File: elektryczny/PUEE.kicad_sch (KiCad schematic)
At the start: 60 parts, among them J1 CAN, J2 LED2, J3 OLED, J4 Button1, J5 LED1, J6 Button1, J7 Conn_01x05, SW1 Button2, SW2 Button1, U1 STM32F042F4Px, U10 WS2815, U11 WS2815, U13 SN65HVD230QDRG4Q1, U2 ESP-12E, U3 TPS54302DDCR, U4 WS2815, U5 WS2815, U6 WS2815, U7 WS2815, U8 WS2815, U9 WS2815, Y2 ABL-8MHZ-B2

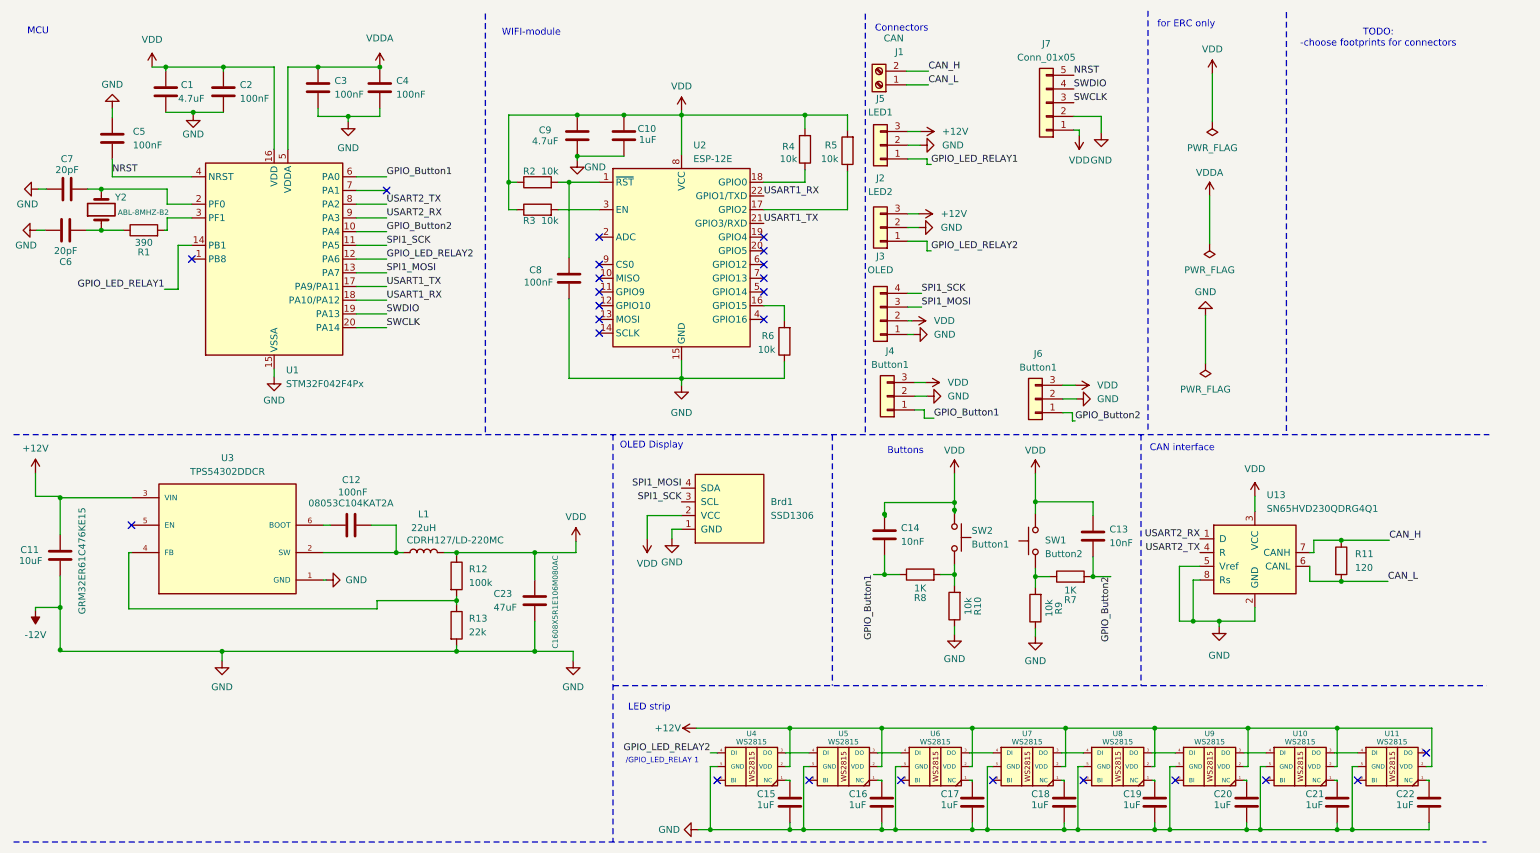
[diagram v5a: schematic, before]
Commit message: poprawa schematu, wymiary sciezek wylotek, pcb film 3.
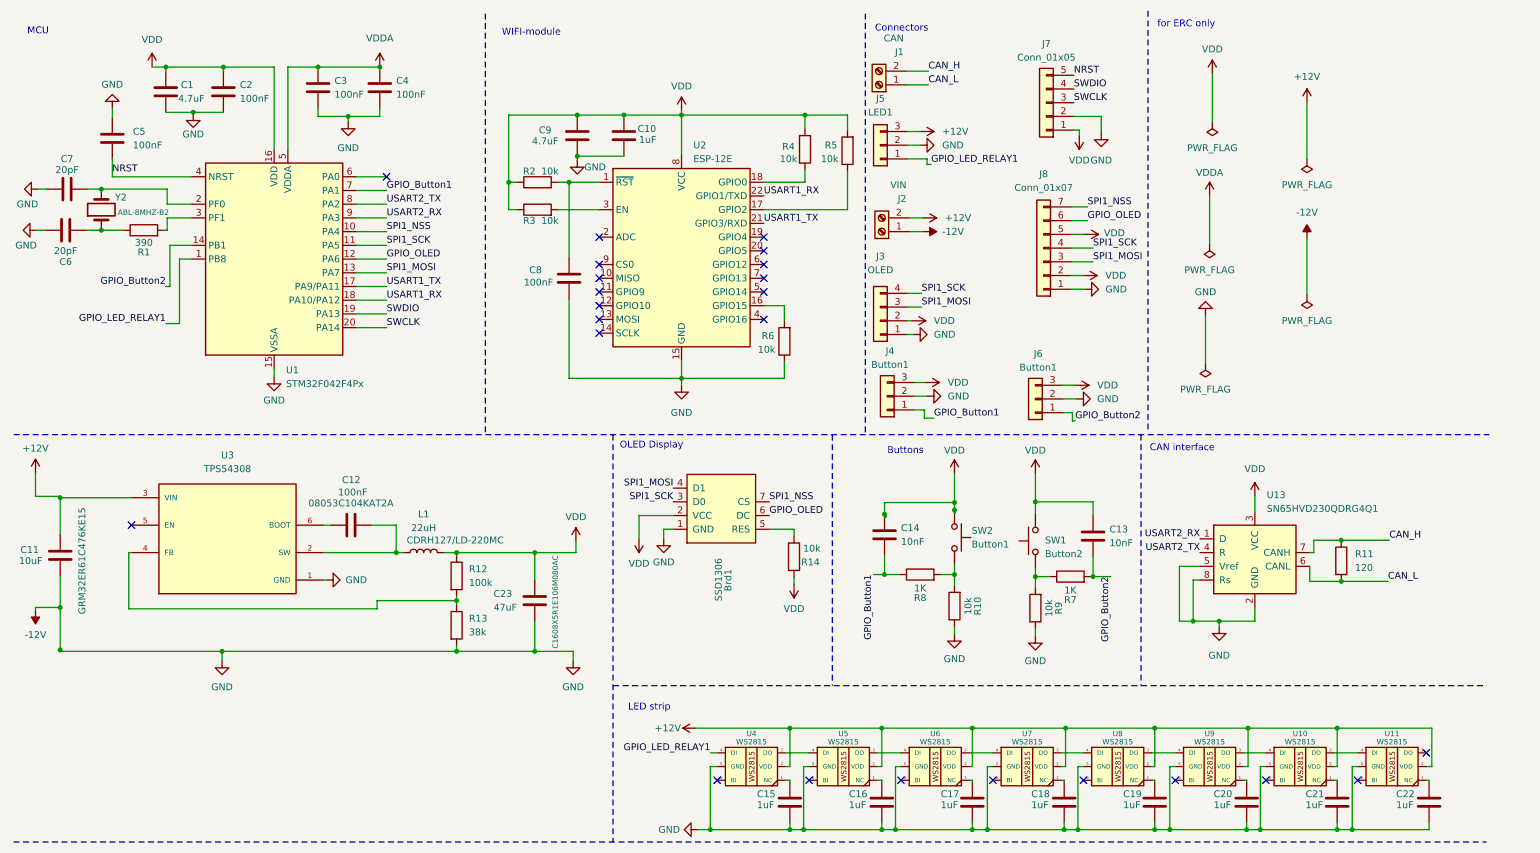
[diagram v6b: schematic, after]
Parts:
- removed J2: LED2, Connector_PinHeader_2.54mm:PinHeader_1x03_P2.54mm_Vertical, symbol Connector_Generic:Conn_01x03
- added J2: VIN, Connector_Phoenix_MC:PhoenixContact_MCV_1,5_2-G-3.5_1x02_P3.50mm_Vertical, symbol Connector:Screw_Terminal_01x02
- added J8: Conn_01x07, Connector_PinHeader_2.54mm:PinHeader_1x07_P2.54mm_Vertical, symbol Connector_Generic:Conn_01x07
- added R14: 10k, Resistor_SMD:R_0805_2012Metric, symbol Device:R
- R13: value 22k -> 38k
- SW1, SW2: footprint (none) -> Button_Switch_SMD:SW_SPST_PTS647_Sx38; Catalogue_number (none) -> PTS647 Series
- U10, U11, U4, U5, U6, U7, U8, U9: footprint WS2815:LED-TRICOLOR-5050 -> LED_SMD:LED_WS2812_PLCC6_5.0x5.0mm_P1.6mm
- U3: value TPS54302DDCR -> TPS54308; footprint TPS54302DDCR:SOT95P280X110-6N -> Package_SO:Texas_HSOP-8-1EP_3.9x4.9mm_P1.27mm
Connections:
- net +12V: now also J2.2 (Pin_2)
- net -12V: now also J2.1 (Pin_1), J8.1 (Pin_1)
- net GPIO_Button1: now also U1.7 (PA1); no longer U1.6 (PA0)
- net GPIO_Button2: now also U1.14 (PB1); no longer U1.10 (PA4)
- net GPIO_LED_RELAY1: now also U1.1 (PB8), U4.4 (DI); no longer U1.14 (PB1)
- net SPI1_MOSI: now also J8.3 (Pin_3)
- net SPI1_SCK: now also J8.4 (Pin_4)
- net VDD: now also J8.2 (Pin_2), J8.5 (Pin_5), R14.2
- net GPIO_LED_RELAY2 renamed GPIO_OLED
- net GPIO_OLED: now also Brd1.6 (DC), J8.6 (Pin_6); no longer U4.4 (DI)
- new net: Brd1.5 (RES), R14.1
- new net SPI1_NSS: Brd1.7 (CS), J8.7 (Pin_7), U1.10 (PA4)
- no-connect marks 25 -> 24
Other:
- note removed: "/GPIO_LED_RELAY 1"
- note removed: "TODO: -choose footprints for connectors"

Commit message: update
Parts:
- removed J3: OLED, Connector_PinHeader_2.54mm:PinHeader_1x04_P2.54mm_Vertical, symbol Connector_Generic:Conn_01x04
- C3: value 100nF -> 10nF
- C4: value 100nF -> 1uF
- J6: value Button1 -> Button2
- J7: value Conn_01x05 -> STM
- J8: value Conn_01x07 -> OLED
- U3: footprint Package_SO:Texas_HSOP-8-1EP_3.9x4.9mm_P1.27mm -> Package_TO_SOT_SMD:SOT-23-6
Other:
- moved on the sheet: J4, J6

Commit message: polaczenia pcb czesc 1/2
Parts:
- Y2: footprint Crystal:Crystal_HC49-U_Vertical -> footprint_oscylator:ABL-8.000MHZ-B2_ABR
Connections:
- net +12V: now also C11.2; no longer C11.1
- net -12V: now also C11.1; no longer C11.2
- net CAN_H: now also R11.2; no longer R11.1
- net CAN_L: now also R11.1; no longer R11.2
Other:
- moved on the sheet: C11, R11
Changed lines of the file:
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@@
 	)
 	(junction
+		(at 258.064 109.728)
+		(diameter 0)
+		(color 0 0 0 0)
+	)
+	(junction
 		(at 240.792 144.526)
 		(diameter 0)
@@
 	)
 	(junction
-		(at 258.064 117.348)
-		(diameter 0)
-		(color 0 0 0 0)
-	)
-	(junction
 		(at 94.234 120.904)
 		(diameter 0)
@@
 	)
 	(junction
-		(at 258.064 109.728)
-		(diameter 0)
-		(color 0 0 0 0)
-	)
-	(junction
 		(at 186.436 104.14)
 		(diameter 0)
@@
 	)
 	(junction
+		(at 258.064 117.348)
+		(diameter 0)
+		(color 0 0 0 0)
+	)
+	(junction
 		(at 201.422 116.459)
 		(diameter 0)
@@
 	(wire
 		(pts
-			(xy 258.064 117.348) (xy 266.7 117.348)
-		)
-		(stroke
-			(width 0)
-			(type default)
-		)
-	)
-	(wire
-		(pts
 			(xy 206.756 75.184) (xy 209.296 75.184)
 		)
@@
 	(wire
 		(pts
-			(xy 258.064 109.728) (xy 266.954 109.728)
-		)
-		(stroke
-			(width 0)
-			(type default)
-		)
-	)
-	(wire
-		(pts
 			(xy 154.94 66.294) (xy 154.94 69.088)
 		)
@@
 	(wire
 		(pts
+			(xy 258.064 117.348) (xy 266.7 117.348)
+		)
+		(stroke
+			(width 0)
+			(type default)
+		)
+	)
+	(wire
+		(pts
 			(xy 183.896 116.078) (xy 186.436 116.078)
 		)
@@
 	(wire
 		(pts
+			(xy 258.064 109.728) (xy 266.954 109.728)
+		)
+		(stroke
+			(width 0)
+			(type default)
+		)
+	)
+	(wire
+		(pts
 			(xy 206.756 162.052) (xy 206.756 163.322)
 		)
@@
 	(symbol
 		(lib_id "Device:C")
-		(at 20.828 112.522 0)
+		(at 20.828 112.522 180)
 		(unit 1)
 		(exclude_from_sim no)
@@
 		(dnp no)
 		(property "Reference" "C11"
-			(at 13.462 111.506 0)
+			(at 28.194 113.538 0)
 			(effects
 				(font
@@
 		)
 		(property "Value" "10uF"
-			(at 13.208 113.538 0)
+			(at 28.448 111.506 0)
 			(effects
 				(font
@@
 		)
 		(property "Footprint" "Capacitor_SMD:C_1210_3225Metric"
-			(at 21.7932 116.332 0)
+			(at 19.8628 108.712 0)
 			(effects
 				(font
@@
 		)
 		(property "Catalogue_number" "GRM32ER61C476KE15"
-			(at 24.892 113.538 90)
+			(at 16.764 111.506 90)
 			(effects
 				(font
@@
 	(symbol
 		(lib_id "Device:R")
-		(at 258.064 113.538 0)
+		(at 258.064 113.538 180)
 		(unit 1)
 		(exclude_from_sim no)
@@
 		(fields_autoplaced yes)
 		(property "Reference" "R11"
-			(at 260.604 112.2679 0)
+			(at 260.35 112.2679 0)
 			(effects
 				(font
 					(size 1.27 1.27)
 				)
-				(justify left)
+				(justify right)
 			)
 		)
 		(property "Value" "120"
-			(at 260.604 114.8079 0)
+			(at 260.35 114.8079 0)
 			(effects
 				(font
 					(size 1.27 1.27)
 				)
-				(justify left)
+				(justify right)
 			)
 		)
 		(property "Footprint" "Resistor_SMD:R_0805_2012Metric"
-			(at 256.286 113.538 90)
+			(at 259.842 113.538 90)
 			(effects
 				(font
@@
 			)
 		)
-		(property "Footprint" "Crystal:Crystal_HC49-U_Vertical"
+		(property "Footprint" "footprint_oscylator:ABL-8.000MHZ-B2_ABR"
 			(at 28.448 48.514 0)
 			(effects
